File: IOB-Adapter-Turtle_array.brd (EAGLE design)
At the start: 106.7 x 104.1 mm, 53 parts

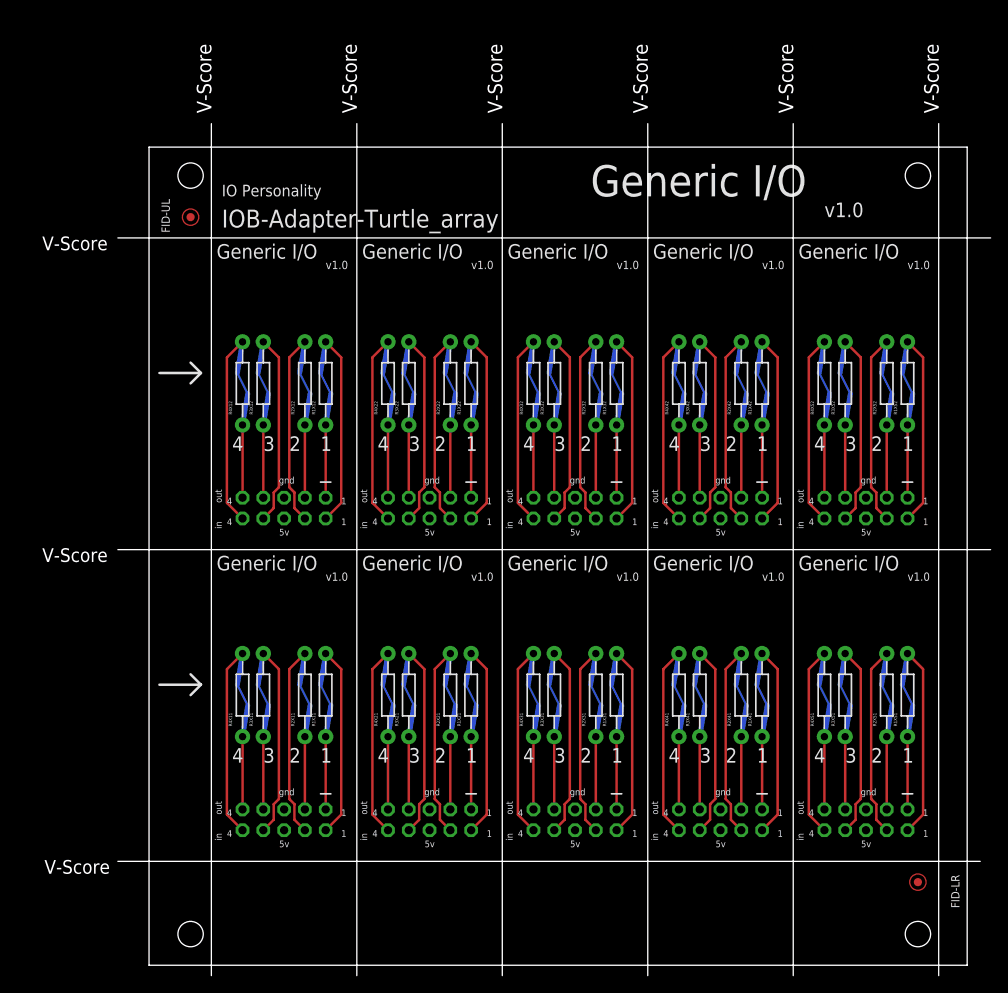
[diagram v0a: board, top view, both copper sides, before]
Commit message: silkscreen tweeks
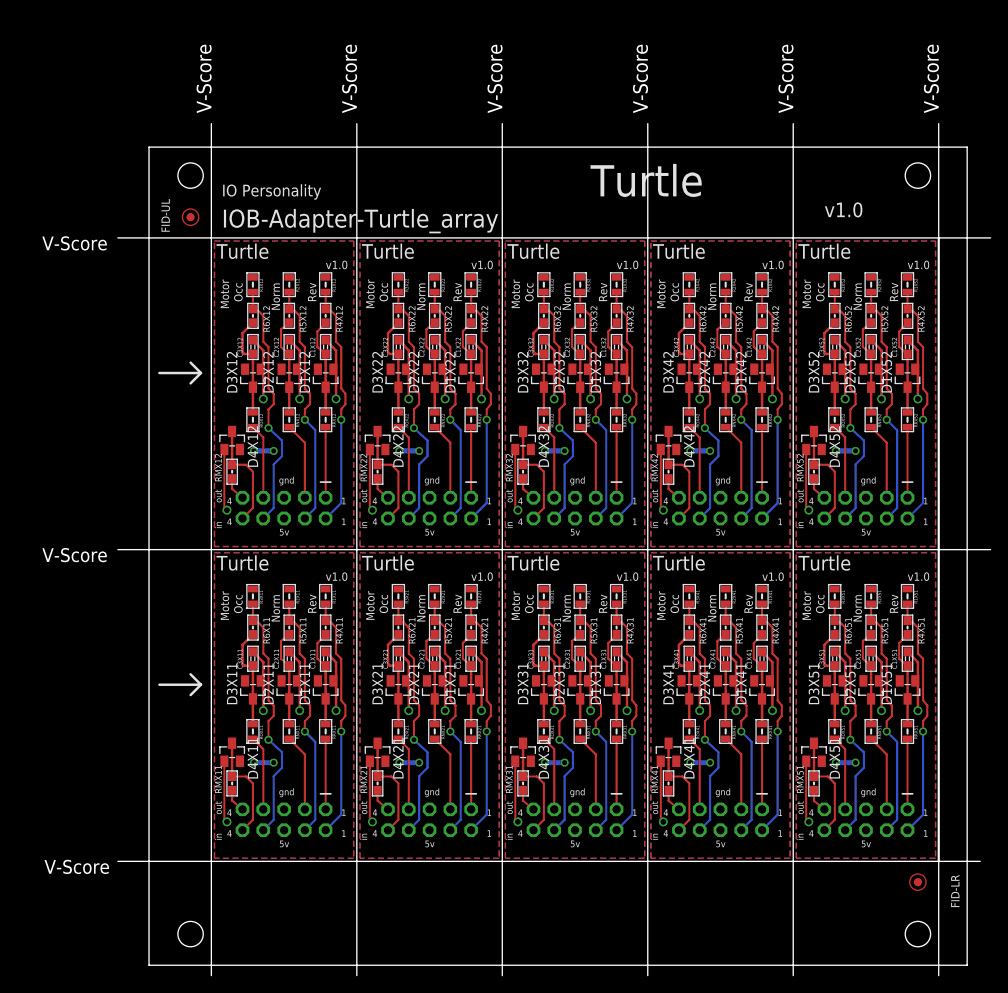
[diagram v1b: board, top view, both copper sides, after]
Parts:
- added C1X11, C1X12, C1X21, C1X22, C1X31, C1X32, C1X41, C1X42, C1X51, C1X52, C2X11, C2X12, C2X21, C2X22, C2X31, C2X32, C2X41, C2X42, C2X51, C2X52, C3X11, C3X12, C3X21, C3X22, C3X31, C3X32, C3X41, C3X42, C3X51, C3X52: 0.01uF, SPCoast:0603-CAP
- added D1X11, D1X12, D1X21, D1X22, D1X31, D1X32, D1X41, D1X42, D1X51, D1X52, D2X11, D2X12, D2X21, D2X22, D2X31, D2X32, D2X41, D2X42, D2X51, D2X52, D3X11, D3X12, D3X21, D3X22, D3X31, D3X32, D3X41, D3X42, D3X51, D3X52: BAT54S, SPCoast:SOT23
- added D4X11, D4X12, D4X21, D4X22, D4X31, D4X32, D4X41, D4X42, D4X51, D4X52: 4.7v, SPCoast:SOT23
- added R5X11, R5X12, R5X21, R5X22, R5X31, R5X32, R5X41, R5X42, R5X51, R5X52, R6X11, R6X12, R6X21, R6X22, R6X31, R6X32, R6X41, R6X42, R6X51, R6X52, RMX11, RMX12, RMX21, RMX22, RMX31, RMX32, RMX41, RMX42, RMX51, RMX52: 1K0, SPCoast:0603-RES
- added RNX11, RNX12, RNX21, RNX22, RNX31, RNX32, RNX41, RNX42, RNX51, RNX52, ROX11, ROX12, ROX21, ROX22, ROX31, ROX32, ROX41, ROX42, ROX51, ROX52, RRX11, RRX12, RRX21, RRX22, RRX31, RRX32, RRX41, RRX42, RRX51, RRX52: 82R, SPCoast:0805-RES
- R1X11, R1X12, R1X21, R1X22, R1X31, R1X32, R1X41, R1X42, R1X51, R1X52, R2X11, R2X12, R2X21, R2X22, R2X31, R2X32, R2X41, R2X42, R2X51, R2X52, R3X11, R3X12, R3X21, R3X22, R3X31, R3X32, R3X41, R3X42, R3X51, R3X52: value NOSTUFF -> 10k; device SPCoast:CUT-R -> SPCoast:0805-RES
- R4X11, R4X12, R4X21, R4X22, R4X31, R4X32, R4X41, R4X42, R4X51, R4X52: value NOSTUFF -> 1K0; device SPCoast:CUT-R -> SPCoast:0603-RES
- moved R4X41 13.1 mm to (74.9, 41.3), turned to 270 degrees
- moved R4X42 13.1 mm to (74.9, 79.4), turned to 270 degrees
- moved R4X11 13.1 mm to (21.6, 41.3), turned to 270 degrees
- moved R4X12 13.1 mm to (21.6, 79.4), turned to 270 degrees
- moved R4X21 13.1 mm to (39.4, 41.3), turned to 270 degrees
- moved R4X22 13.1 mm to (39.4, 79.4), turned to 270 degrees
- moved R4X31 13.1 mm to (57.1, 41.3), turned to 270 degrees
- moved R4X32 13.1 mm to (57.1, 79.4), turned to 270 degrees
- moved R4X51 13.1 mm to (92.7, 41.3), turned to 270 degrees
- moved R4X52 13.1 mm to (92.7, 79.4), turned to 270 degrees
- moved R2X11 12.2 mm to (17.1, 45.1), turned to 270 degrees
- moved R2X12 12.2 mm to (17.1, 83.2), turned to 270 degrees
- moved R2X21 12.2 mm to (34.9, 45.1), turned to 270 degrees
- moved R2X22 12.2 mm to (34.9, 83.2), turned to 270 degrees
- moved R2X31 12.2 mm to (52.7, 45.1), turned to 270 degrees
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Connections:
- removed net N$1X11: JP1X11.1, R1X11.P2
- removed net N$1X12: JP1X12.1, R1X12.P2
- removed net N$1X21: JP1X21.1, R1X21.P2
- removed net N$1X22: JP1X22.1, R1X22.P2
- removed net N$1X31: JP1X31.1, R1X31.P2
- removed net N$1X32: JP1X32.1, R1X32.P2
- removed net N$1X41: JP1X41.1, R1X41.P2
- removed net N$1X42: JP1X42.1, R1X42.P2
- removed net N$1X51: JP1X51.1, R1X51.P2
- removed net N$1X52: JP1X52.1, R1X52.P2
- removed net N$4X11: JP1X11.9, R4X11.P2
- removed net N$4X12: JP1X12.9, R4X12.P2
- removed net N$4X21: JP1X21.9, R4X21.P2
- removed net N$4X22: JP1X22.9, R4X22.P2
- removed net N$4X31: JP1X31.9, R4X31.P2
- removed net N$4X32: JP1X32.9, R4X32.P2
- removed net N$4X41: JP1X41.9, R4X41.P2
- removed net N$4X42: JP1X42.9, R4X42.P2
- removed net N$4X51: JP1X51.9, R4X51.P2
- removed net N$4X52: JP1X52.9, R4X52.P2
- new net IO1X11: JP1X11.1, RRX11.2
- new net IO1X12: JP1X12.1, RRX12.2
- new net IO1X21: JP1X21.1, RRX21.2
- new net IO1X22: JP1X22.1, RRX22.2
- new net IO1X31: JP1X31.1, RRX31.2
- new net IO1X32: JP1X32.1, RRX32.2
- new net IO1X41: JP1X41.1, RRX41.2
- new net IO1X42: JP1X42.1, RRX42.2
- new net IO1X51: JP1X51.1, RRX51.2
- new net IO1X52: JP1X52.1, RRX52.2
- new net IO2X11: JP1X11.3, RNX11.2
- new net IO2X12: JP1X12.3, RNX12.2
- new net IO2X21: JP1X21.3, RNX21.2
- new net IO2X22: JP1X22.3, RNX22.2
- new net IO2X31: JP1X31.3, RNX31.2
- new net IO2X32: JP1X32.3, RNX32.2
- new net IO2X41: JP1X41.3, RNX41.2
- new net IO2X42: JP1X42.3, RNX42.2
- new net IO2X51: JP1X51.3, RNX51.2
- new net IO2X52: JP1X52.3, RNX52.2
- new net IO3X11: JP1X11.7, ROX11.2
- new net IO3X12: JP1X12.7, ROX12.2
- new net IO3X21: JP1X21.7, ROX21.2
- new net IO3X22: JP1X22.7, ROX22.2
- new net IO3X31: JP1X31.7, ROX31.2
- new net IO3X32: JP1X32.7, ROX32.2
- new net IO3X41: JP1X41.7, ROX41.2
- new net IO3X42: JP1X42.7, ROX42.2
- new net IO3X51: JP1X51.7, ROX51.2
- new net IO3X52: JP1X52.7, ROX52.2
- new net IO4X11: JP1X11.9, RMX11.1
- new net IO4X12: JP1X12.9, RMX12.1
- new net IO4X21: JP1X21.9, RMX21.1
- new net IO4X22: JP1X22.9, RMX22.1
- new net IO4X31: JP1X31.9, RMX31.1
- new net IO4X32: JP1X32.9, RMX32.1
- new net IO4X41: JP1X41.9, RMX41.1
- new net IO4X42: JP1X42.9, RMX42.1
- new net IO4X51: JP1X51.9, RMX51.1
- new net IO4X52: JP1X52.9, RMX52.1
- new net N$14X11: C3X11.1, D3X11.3, R6X11.2, ROX11.1
- new net N$14X12: C3X12.1, D3X12.3, R6X12.2, ROX12.1
- new net N$14X21: C3X21.1, D3X21.3, R6X21.2, ROX21.1
- new net N$14X22: C3X22.1, D3X22.3, R6X22.2, ROX22.1
- new net N$14X31: C3X31.1, D3X31.3, R6X31.2, ROX31.1
- new net N$14X32: C3X32.1, D3X32.3, R6X32.2, ROX32.1
- new net N$14X41: C3X41.1, D3X41.3, R6X41.2, ROX41.1
- new net N$14X42: C3X42.1, D3X42.3, R6X42.2, ROX42.1
- new net N$14X51: C3X51.1, D3X51.3, R6X51.2, ROX51.1
- new net N$14X52: C3X52.1, D3X52.3, R6X52.2, ROX52.1
- net GNDX11: now also C1X11.2, C2X11.2, C3X11.2, D1X11.1, D2X11.1, D3X11.1, D4X11.1
- net GNDX12: now also C1X12.2, C2X12.2, C3X12.2, D1X12.1, D2X12.1, D3X12.1, D4X12.1
- net GNDX21: now also C1X21.2, C2X21.2, C3X21.2, D1X21.1, D2X21.1, D3X21.1, D4X21.1
- net GNDX22: now also C1X22.2, C2X22.2, C3X22.2, D1X22.1, D2X22.1, D3X22.1, D4X22.1
- net GNDX31: now also C1X31.2, C2X31.2, C3X31.2, D1X31.1, D2X31.1, D3X31.1, D4X31.1
- net GNDX32: now also C1X32.2, C2X32.2, C3X32.2, D1X32.1, D2X32.1, D3X32.1, D4X32.1
- net GNDX41: now also C1X41.2, C2X41.2, C3X41.2, D1X41.1, D2X41.1, D3X41.1, D4X41.1
- net GNDX42: now also C1X42.2, C2X42.2, C3X42.2, D1X42.1, D2X42.1, D3X42.1, D4X42.1
- net GNDX51: now also C1X51.2, C2X51.2, C3X51.2, D1X51.1, D2X51.1, D3X51.1, D4X51.1
- net GNDX52: now also C1X52.2, C2X52.2, C3X52.2, D1X52.1, D2X52.1, D3X52.1, D4X52.1
- net N$2X11: now also C2X11.1, D2X11.3, R5X11.2, RNX11.1; no longer JP1X11.3, R2X11.P2
- net N$2X12: now also C2X12.1, D2X12.3, R5X12.2, RNX12.1; no longer JP1X12.3, R2X12.P2
- net N$2X21: now also C2X21.1, D2X21.3, R5X21.2, RNX21.1; no longer JP1X21.3, R2X21.P2
- net N$2X22: now also C2X22.1, D2X22.3, R5X22.2, RNX22.1; no longer JP1X22.3, R2X22.P2
- net N$2X31: now also C2X31.1, D2X31.3, R5X31.2, RNX31.1; no longer JP1X31.3, R2X31.P2
- net N$2X32: now also C2X32.1, D2X32.3, R5X32.2, RNX32.1; no longer JP1X32.3, R2X32.P2
- net N$2X41: now also C2X41.1, D2X41.3, R5X41.2, RNX41.1; no longer JP1X41.3, R2X41.P2
- net N$2X42: now also C2X42.1, D2X42.3, R5X42.2, RNX42.1; no longer JP1X42.3, R2X42.P2
- net N$2X51: now also C2X51.1, D2X51.3, R5X51.2, RNX51.1; no longer JP1X51.3, R2X51.P2
- net N$2X52: now also C2X52.1, D2X52.3, R5X52.2, RNX52.1; no longer JP1X52.3, R2X52.P2
- net N$3X11: now also C1X11.1, D1X11.3, R4X11.2, RRX11.1; no longer JP1X11.7, R3X11.P2
- net N$3X12: now also C1X12.1, D1X12.3, R4X12.2, RRX12.1; no longer JP1X12.7, R3X12.P2
- net N$3X21: now also C1X21.1, D1X21.3, R4X21.2, RRX21.1; no longer JP1X21.7, R3X21.P2
- net N$3X22: now also C1X22.1, D1X22.3, R4X22.2, RRX22.1; no longer JP1X22.7, R3X22.P2
- net N$3X31: now also C1X31.1, D1X31.3, R4X31.2, RRX31.1; no longer JP1X31.7, R3X31.P2
- net N$3X32: now also C1X32.1, D1X32.3, R4X32.2, RRX32.1; no longer JP1X32.7, R3X32.P2
- net N$3X41: now also C1X41.1, D1X41.3, R4X41.2, RRX41.1; no longer JP1X41.7, R3X41.P2
- net N$3X42: now also C1X42.1, D1X42.3, R4X42.2, RRX42.1; no longer JP1X42.7, R3X42.P2
- net N$3X51: now also C1X51.1, D1X51.3, R4X51.2, RRX51.1; no longer JP1X51.7, R3X51.P2
- net N$3X52: now also C1X52.1, D1X52.3, R4X52.2, RRX52.1; no longer JP1X52.7, R3X52.P2
- net P1X11: now also R1X11.2, R4X11.1; no longer R1X11.P1
- net P1X12: now also R1X12.2, R4X12.1; no longer R1X12.P1
- net P1X21: now also R1X21.2, R4X21.1; no longer R1X21.P1
- net P1X22: now also R1X22.2, R4X22.1; no longer R1X22.P1
- net P1X31: now also R1X31.2, R4X31.1; no longer R1X31.P1
- net P1X32: now also R1X32.2, R4X32.1; no longer R1X32.P1
- net P1X41: now also R1X41.2, R4X41.1; no longer R1X41.P1
- net P1X42: now also R1X42.2, R4X42.1; no longer R1X42.P1
- net P1X51: now also R1X51.2, R4X51.1; no longer R1X51.P1
- net P1X52: now also R1X52.2, R4X52.1; no longer R1X52.P1
- net P2X11: now also R2X11.2, R5X11.1; no longer R2X11.P1
- net P2X12: now also R2X12.2, R5X12.1; no longer R2X12.P1
- net P2X21: now also R2X21.2, R5X21.1; no longer R2X21.P1
- net P2X22: now also R2X22.2, R5X22.1; no longer R2X22.P1
- net P2X31: now also R2X31.2, R5X31.1; no longer R2X31.P1
- net P2X32: now also R2X32.2, R5X32.1; no longer R2X32.P1
- net P2X41: now also R2X41.2, R5X41.1; no longer R2X41.P1
- net P2X42: now also R2X42.2, R5X42.1; no longer R2X42.P1
- net P2X51: now also R2X51.2, R5X51.1; no longer R2X51.P1
- net P2X52: now also R2X52.2, R5X52.1; no longer R2X52.P1
- net P3X11: now also R3X11.2, R6X11.1; no longer R3X11.P1
- net P3X12: now also R3X12.2, R6X12.1; no longer R3X12.P1
- net P3X21: now also R3X21.2, R6X21.1; no longer R3X21.P1
- net P3X22: now also R3X22.2, R6X22.1; no longer R3X22.P1
- net P3X31: now also R3X31.2, R6X31.1; no longer R3X31.P1
- net P3X32: now also R3X32.2, R6X32.1; no longer R3X32.P1
- net P3X41: now also R3X41.2, R6X41.1; no longer R3X41.P1
- net P3X42: now also R3X42.2, R6X42.1; no longer R3X42.P1
- net P3X51: now also R3X51.2, R6X51.1; no longer R3X51.P1
- net P3X52: now also R3X52.2, R6X52.1; no longer R3X52.P1
- net P4X11: now also D4X11.3, RMX11.2; no longer R4X11.P1
- net P4X12: now also D4X12.3, RMX12.2; no longer R4X12.P1
- net P4X21: now also D4X21.3, RMX21.2; no longer R4X21.P1
- net P4X22: now also D4X22.3, RMX22.2; no longer R4X22.P1
- net P4X31: now also D4X31.3, RMX31.2; no longer R4X31.P1
- net P4X32: now also D4X32.3, RMX32.2; no longer R4X32.P1
- net P4X41: now also D4X41.3, RMX41.2; no longer R4X41.P1
- net P4X42: now also D4X42.3, RMX42.2; no longer R4X42.P1
- net P4X51: now also D4X51.3, RMX51.2; no longer R4X51.P1
- net P4X52: now also D4X52.3, RMX52.2; no longer R4X52.P1
- net VCCX11: now also D1X11.2, D2X11.2, D3X11.2, R1X11.1, R2X11.1, R3X11.1
- net VCCX12: now also D1X12.2, D2X12.2, D3X12.2, R1X12.1, R2X12.1, R3X12.1
- net VCCX21: now also D1X21.2, D2X21.2, D3X21.2, R1X21.1, R2X21.1, R3X21.1
- net VCCX22: now also D1X22.2, D2X22.2, D3X22.2, R1X22.1, R2X22.1, R3X22.1
- net VCCX31: now also D1X31.2, D2X31.2, D3X31.2, R1X31.1, R2X31.1, R3X31.1
- net VCCX32: now also D1X32.2, D2X32.2, D3X32.2, R1X32.1, R2X32.1, R3X32.1
- net VCCX41: now also D1X41.2, D2X41.2, D3X41.2, R1X41.1, R2X41.1, R3X41.1
- net VCCX42: now also D1X42.2, D2X42.2, D3X42.2, R1X42.1, R2X42.1, R3X42.1
- net VCCX51: now also D1X51.2, D2X51.2, D3X51.2, R1X51.1, R2X51.1, R3X51.1
- net VCCX52: now also D1X52.2, D2X52.2, D3X52.2, R1X52.1, R2X52.1, R3X52.1
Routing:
- net GNDX51: track 0.00 -> 32.5 mm, vias 0 -> 4
- net GNDX52: track 0.00 -> 32.5 mm, vias 0 -> 4
- net GNDX41: track 0.00 -> 32.5 mm, vias 0 -> 4
- net GNDX21: track 0.00 -> 32.5 mm, vias 0 -> 4
- net GNDX31: track 0.00 -> 32.5 mm, vias 0 -> 4
- net GNDX11: track 0.00 -> 32.5 mm, vias 0 -> 4
- net GNDX32: track 0.00 -> 32.5 mm, vias 0 -> 4
- net GNDX22: track 0.00 -> 32.5 mm, vias 0 -> 4
- net GNDX42: track 0.00 -> 32.5 mm, vias 0 -> 4
- net GNDX12: track 0.00 -> 32.5 mm, vias 0 -> 4
- net N$14X42: track 0.00 -> 12.6 mm
- net N$14X41: track 0.00 -> 12.6 mm
- net N$14X21: track 0.00 -> 12.6 mm
- net N$14X11: track 0.00 -> 12.6 mm
- net N$14X22: track 0.00 -> 12.6 mm
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- added copper zone on layer 16, net GNDX11
- added copper zone on layer 16, net GNDX12
- added copper zone on layer 16, net GNDX21
- added copper zone on layer 16, net GNDX22
- added copper zone on layer 16, net GNDX31
- added copper zone on layer 16, net GNDX32
- added copper zone on layer 16, net GNDX41
- added copper zone on layer 16, net GNDX42
- added copper zone on layer 16, net GNDX51
- added copper zone on layer 16, net GNDX52
- added copper zone on layer 1, net VCCX11
- added copper zone on layer 1, net VCCX12
- added copper zone on layer 1, net VCCX21
- added copper zone on layer 1, net VCCX22
- added copper zone on layer 1, net VCCX31
- added copper zone on layer 1, net VCCX32
- added copper zone on layer 1, net VCCX41
- added copper zone on layer 1, net VCCX42
- added copper zone on layer 1, net VCCX51
- added copper zone on layer 1, net VCCX52
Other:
- board text added: "C1"
- board text added: "C2"
- board text added: "C3"
- board text added: "D1"
- board text added: "D2"
- board text added: "D3"
- board text added: "D4"
- board text added: "Green"
- board text added: "Motor"
- board text added: "Norm"
- board text added: "Occ"
- board text added: "R5"
- board text added: "R6"
- board text added: "RM"
- board text added: "RN"
- board text added: "RO"
- board text added: "RR"
- board text added: "Rev"
- board text added: "Turtle"
- board text removed: "1"
- board text removed: "2"
- board text removed: "3"
- board text removed: "4"
- board text removed: "Cut traces if using resistors"
- board text removed: "GENERIC I/O"
- board text removed: "Generic I/O"
- board text removed: "Yellow"

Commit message: added values for connectors
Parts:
- CARRIER: value (none) -> 10x10
- FID-LR, FID-UL: value (none) -> FIDUCIAL
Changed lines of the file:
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@@
 <element name="ROX52" library="SPCoast" package="0805-RES" value="82R" x="83.82" y="66.675" rot="R270"/>
 <element name="RRX52" library="SPCoast" package="0805-RES" value="82R" x="92.71" y="66.675" rot="R270"/>
-<element name="CARRIER" library="SPCoast" package="BOARD-DINRAIL-3.17IN-5X2-IOP" value="" x="0" y="0"/>
-<element name="FID-UL" library="SPCoast" package="FIDUCIAL_1MM" value="" x="5.08" y="91.44" smashed="yes">
+<element name="CARRIER" library="SPCoast" package="BOARD-DINRAIL-3.17IN-5X2-IOP" value="10x10" x="0" y="0"/>
+<element name="FID-UL" library="SPCoast" package="FIDUCIAL_1MM" value="FIDUCIAL" x="5.08" y="91.44" smashed="yes">
 <attribute name="NAME" x="2.54" y="89.535" size="1.016" layer="25" rot="R90"/>
 </element>
-<element name="FID-LR" library="SPCoast" package="FIDUCIAL_1MM" value="" x="93.98" y="10.16" smashed="yes">
+<element name="FID-LR" library="SPCoast" package="FIDUCIAL_1MM" value="FIDUCIAL" x="93.98" y="10.16" smashed="yes">
 <attribute name="NAME" x="99.06" y="6.985" size="1.016" layer="25" rot="R90"/>
 </element>

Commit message: normalized values
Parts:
- CARRIER: value 10x10 -> BOARD
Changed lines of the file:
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@@
 <element name="ROX52" library="SPCoast" package="0805-RES" value="82R" x="83.82" y="66.675" rot="R270"/>
 <element name="RRX52" library="SPCoast" package="0805-RES" value="82R" x="92.71" y="66.675" rot="R270"/>
-<element name="CARRIER" library="SPCoast" package="BOARD-DINRAIL-3.17IN-5X2-IOP" value="10x10" x="0" y="0"/>
+<element name="CARRIER" library="SPCoast" package="BOARD-DINRAIL-3.17IN-5X2-IOP" value="BOARD" x="0" y="0"/>
 <element name="FID-UL" library="SPCoast" package="FIDUCIAL_1MM" value="FIDUCIAL" x="5.08" y="91.44" smashed="yes">
 <attribute name="NAME" x="2.54" y="89.535" size="1.016" layer="25" rot="R90"/>
